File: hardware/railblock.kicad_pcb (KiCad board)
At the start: 2 copper layers, 73 x 87 mm, 38 parts, among them J1 8P8C, J2 8P8C, J3 Conn_01x08_Socket, J4 Conn_01x03_Socket, J5 Conn_01x03_Socket, J6 Conn_01x03_Socket, U1 PESD2CAN, U2 MCP2562-E-SN, U3 ESP32-WROOM-32, U4 ULN2003A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

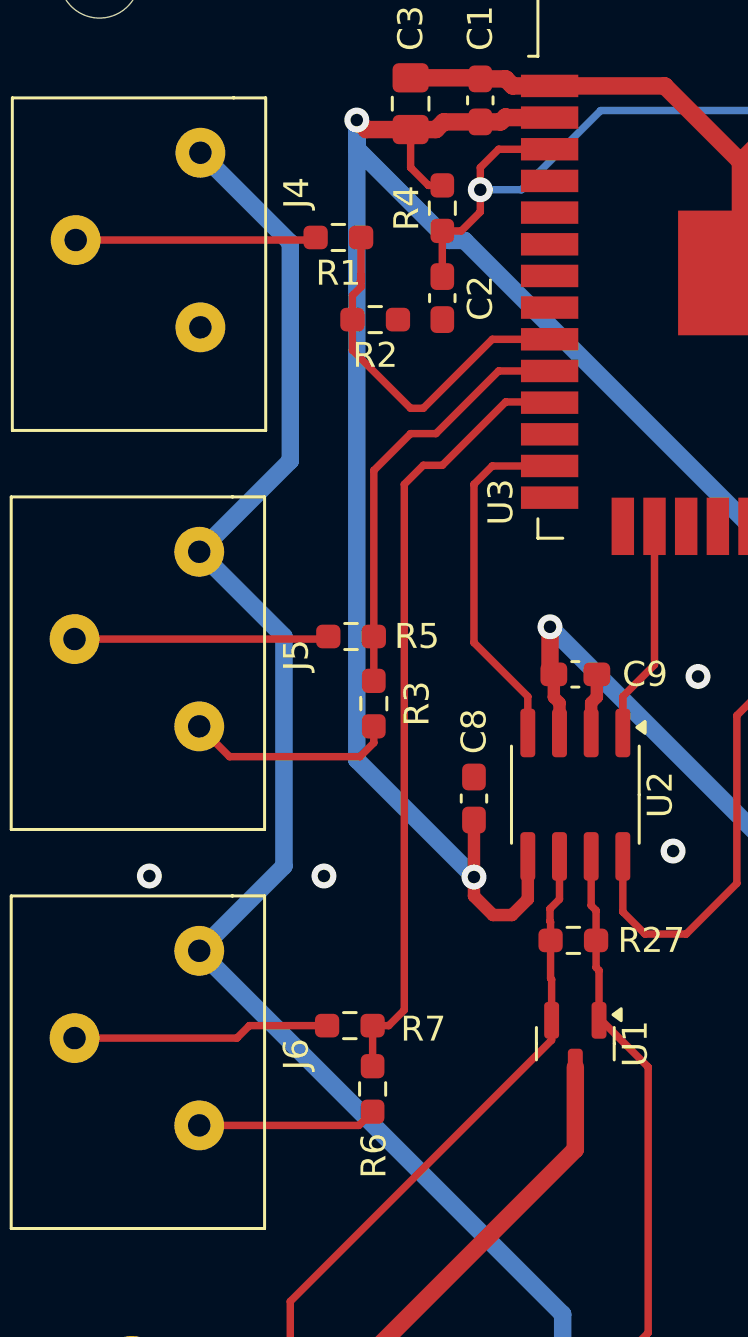
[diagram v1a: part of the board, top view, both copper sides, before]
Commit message: fix: Add pull-up for hall sensors
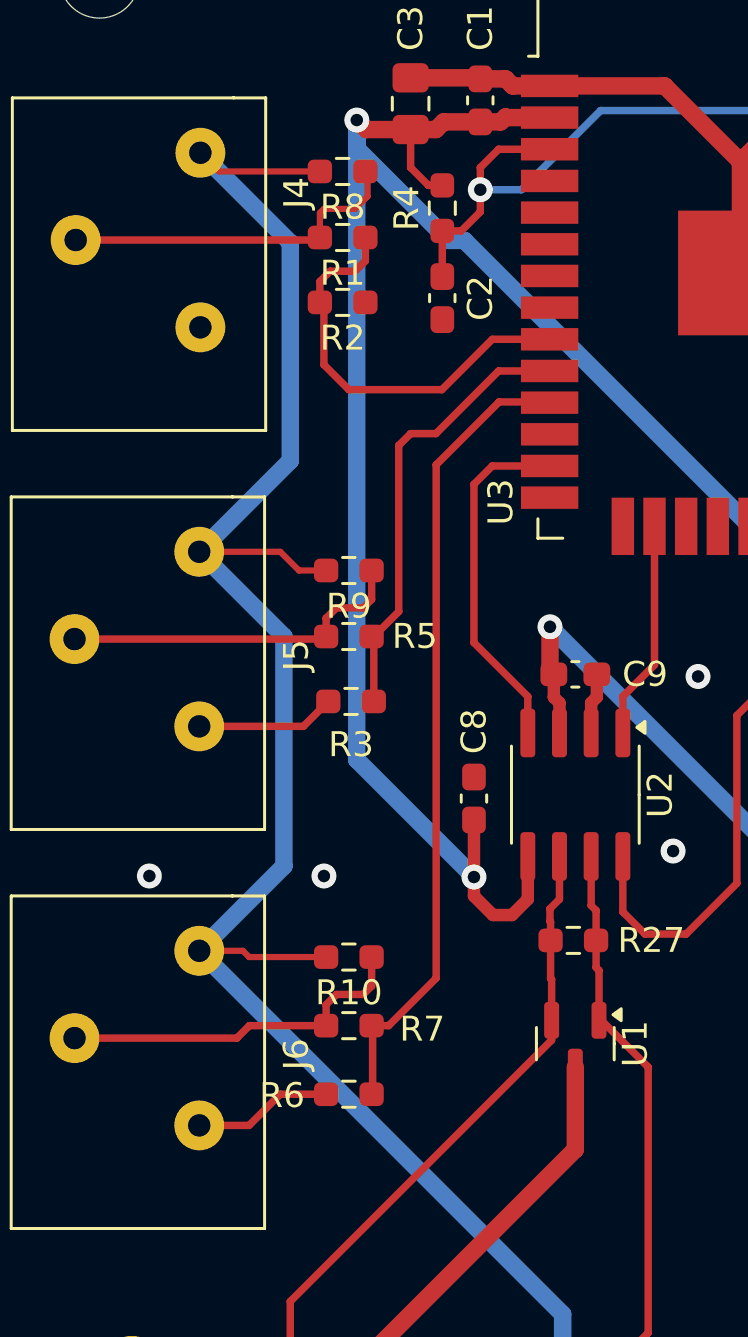
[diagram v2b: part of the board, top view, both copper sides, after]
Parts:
- added R10: 10K, Resistor_SMD:R_0603_1608Metric_Pad0.98x0.95mm_HandSolder, F.Cu at (123.0, 85.2)
- added R8: 10K, Resistor_SMD:R_0603_1608Metric_Pad0.98x0.95mm_HandSolder, F.Cu at (122.8, 53.8)
- added R9: 10K, Resistor_SMD:R_0603_1608Metric_Pad0.98x0.95mm_HandSolder, F.Cu at (123.0, 69.8)
- moved R2 1.48 mm to (122.8, 59.0)
- moved R6 0.97 mm to (123.0, 90.8), turned to 0 degrees
- moved R3 0.92 mm to (123.1, 75.0), turned to 0 degrees
- moved R1 0.17 mm to (122.8, 56.4)
- moved R5 0.09 mm to (123.0, 72.4)
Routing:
- net +12V: track 213.5 -> 229.2 mm
- net Net-(J4-Pin_2): track 9.66 -> 14.0 mm
- net GND: track 123.4 -> 119.0 mm
- net Net-(J6-Pin_2): track 10.3 -> 14.4 mm
- net Net-(J5-Pin_2): track 10.2 -> 14.2 mm
- net Net-(U3-IO33): track 15.0 -> 17.1 mm
- net Net-(U3-IO25): track 17.1 -> 18.1 mm
- net Net-(U3-IO26): track 31.4 -> 32.3 mm

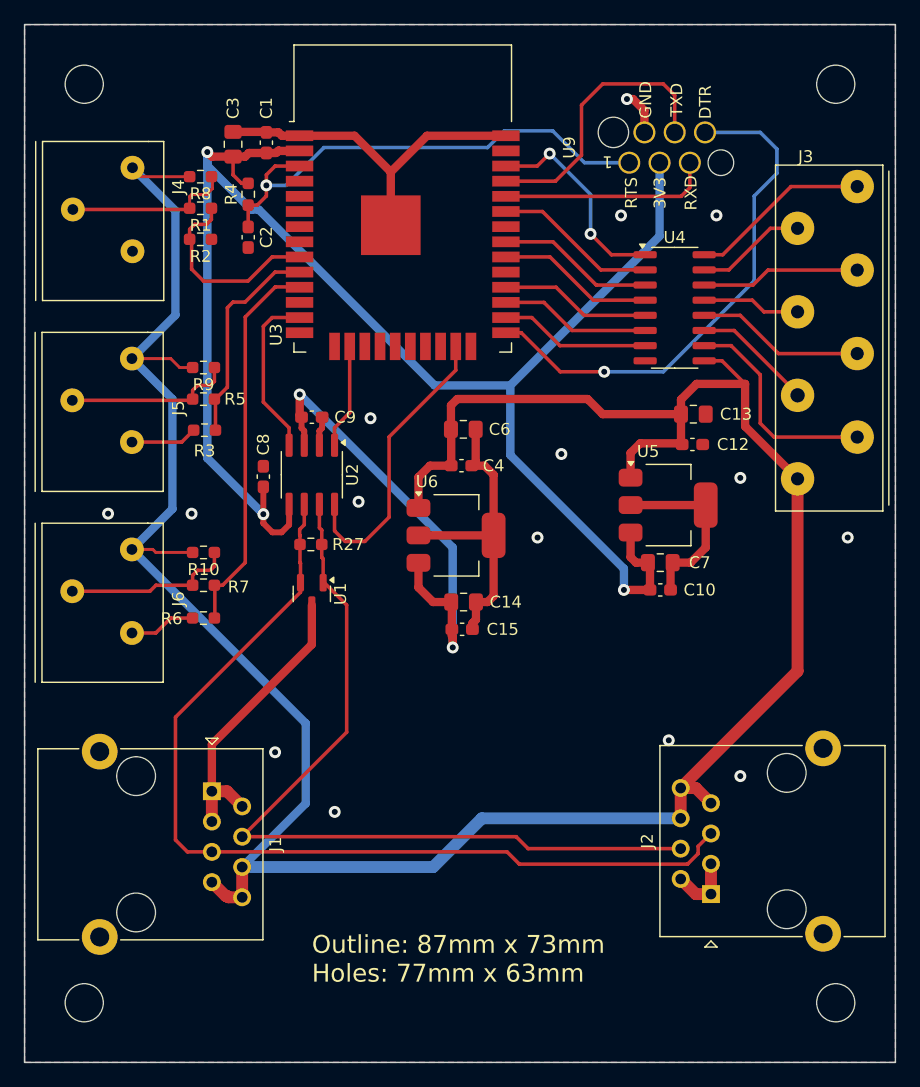
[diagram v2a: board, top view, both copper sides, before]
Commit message: feat: Add JTAG interface
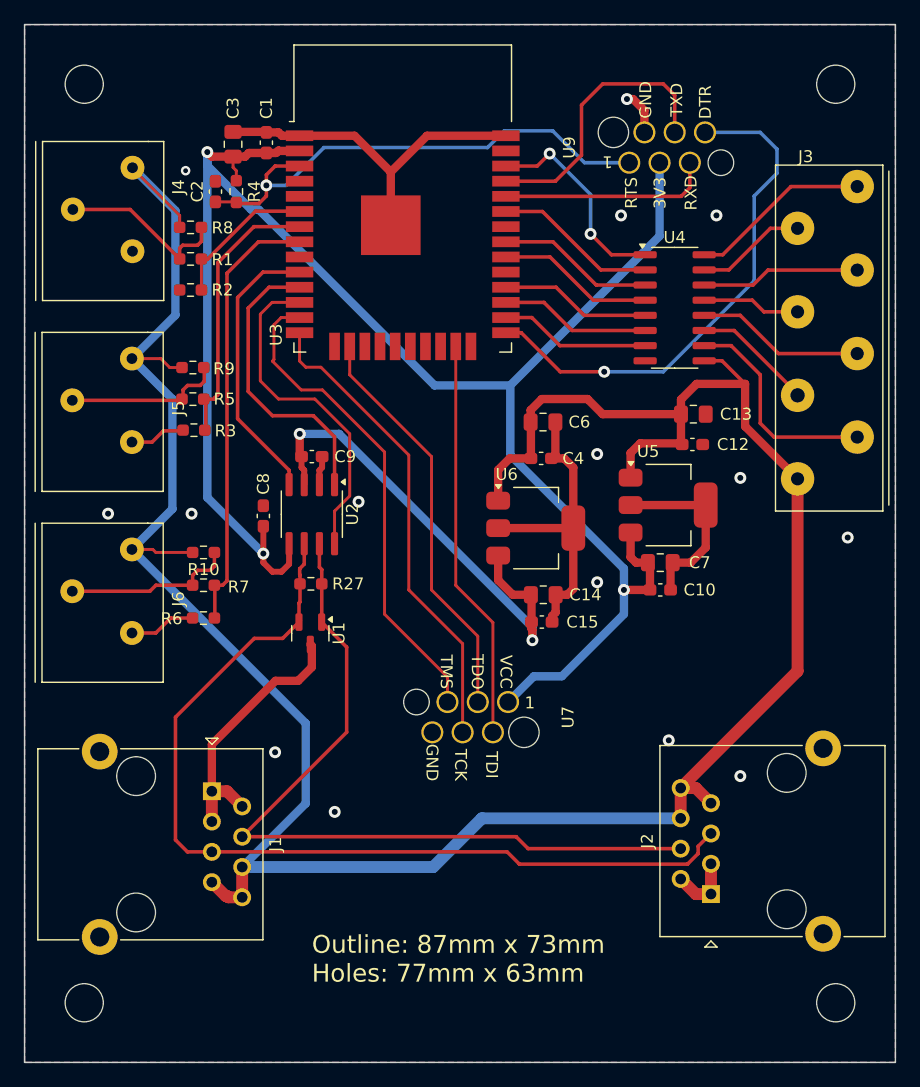
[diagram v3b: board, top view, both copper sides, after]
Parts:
- added U7: wuerthJTAG, awesome:wuerthJTAG, F.Cu at (145.4, 99.1)
- moved C6 6.71 mm to (151.5, 74.3)
- moved C14 6.71 mm to (151.5, 88.8)
- moved C15 6.71 mm to (151.4, 91.1)
- moved C4 6.71 mm to (151.3, 77.4)
- moved U6 6.71 mm to (150.8, 83.2)
- moved C2 4.71 mm to (124.0, 55.0), turned to 90 degrees
- moved R1 4.33 mm to (121.9, 60.6)
- moved R2 4.33 mm to (121.9, 63.2), turned to 0 degrees
- moved R8 4.33 mm to (121.9, 58.0)
- moved U1 3.30 mm to (132.0, 92.0)
- moved R27 3.30 mm to (132.0, 87.9)
- moved U2 3.30 mm to (132.1, 82.0)
- moved C8 3.30 mm to (128.0, 82.2)
- moved C9 3.30 mm to (132.1, 77.2)
- moved R4 1.02 mm to (125.8, 55.0)
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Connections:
- R1 pad 1: Net-(U3-IO33) -> Net-(U3-IO34)
- R2 pad 2: Net-(U3-IO33) -> Net-(U3-IO34)
- R3 pad 2: Net-(U3-IO25) -> Net-(U3-IO35)
- R5 pad 1: Net-(U3-IO25) -> Net-(U3-IO35)
- R6 pad 2: Net-(U3-IO26) -> Net-(U3-IO32)
- R7 pad 1: Net-(U3-IO26) -> Net-(U3-IO32)
- U3 pad 10: Net-(U3-IO25) -> /CAN_RXD
- U3 pad 11: Net-(U3-IO26) -> /CAN_TXD
- U3 pad 12: unconnected-(U3-IO27-Pad12) -> /STDBY
- U3 pad 13: /CAN_RXD -> /TMS
- U3 pad 14: unconnected-(U3-IO12-Pad14) -> /TDI
- U3 pad 16: /CAN_TXD -> /TCK
- U3 pad 23: /STDBY -> /TDO
- U3 pad 6: unconnected-(U3-IO34-Pad6) -> Net-(U3-IO34)
- U3 pad 7: unconnected-(U3-IO35-Pad7) -> Net-(U3-IO35)
- U3 pad 8: unconnected-(U3-IO32-Pad8) -> Net-(U3-IO32)
- U3 pad 9: Net-(U3-IO33) -> unconnected-(U3-IO33-Pad9)
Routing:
- net /TMS: track 0.00 -> 41.2 mm
- net /TDI: track 0.00 -> 39.9 mm
- net Net-(U3-IO32): track 0.00 -> 36.9 mm
- net /TCK: track 0.00 -> 34.3 mm
- net /TDO: track 0.00 -> 33.6 mm
- net Net-(U3-IO26): track 32.3 -> 0.00 mm
- net Net-(U3-IO35): track 0.00 -> 23.4 mm
- net Net-(U3-IO25): track 18.1 -> 0.00 mm
- net +3V3: track 138.4 -> 155.5 mm
- net Net-(U3-IO33): track 17.1 -> 0.00 mm
- net /CAN_TXD: track 8.81 -> 24.9 mm
- net Net-(U3-IO34): track 0.00 -> 12.5 mm
- net /CAN_RXD: track 14.2 -> 23.6 mm
- net +12V: track 229.2 -> 222.3 mm
- net /STDBY: track 24.6 -> 28.4 mm
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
